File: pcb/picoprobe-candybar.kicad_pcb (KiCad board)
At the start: 2 copper layers, 27.9 x 95 mm, 50 parts, among them J0 SWD-UART_PicoprobeCandybar, J1 PinHeader_2x04, J2 PinSocket_1x03, J3 PinSocket_1x02, J4 PinSocket_1x03, J5 PinSocket_1x03, J6 PinSocket_1x03, J7 PinSocket_1x02, Q1 T2N7002AK, Q2 DMP31D1U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

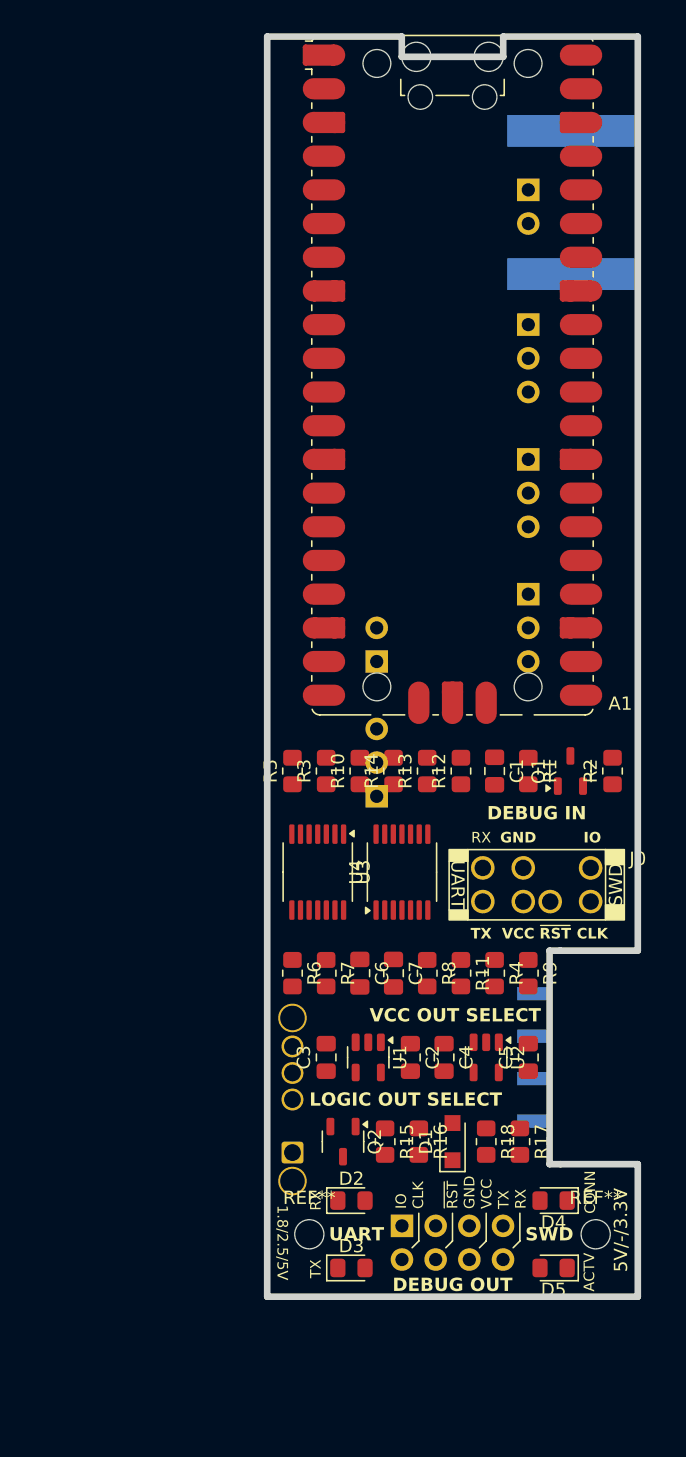
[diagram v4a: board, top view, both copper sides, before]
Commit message: Expand mounting hole copper clearance
Also adjusts some silkscreen text
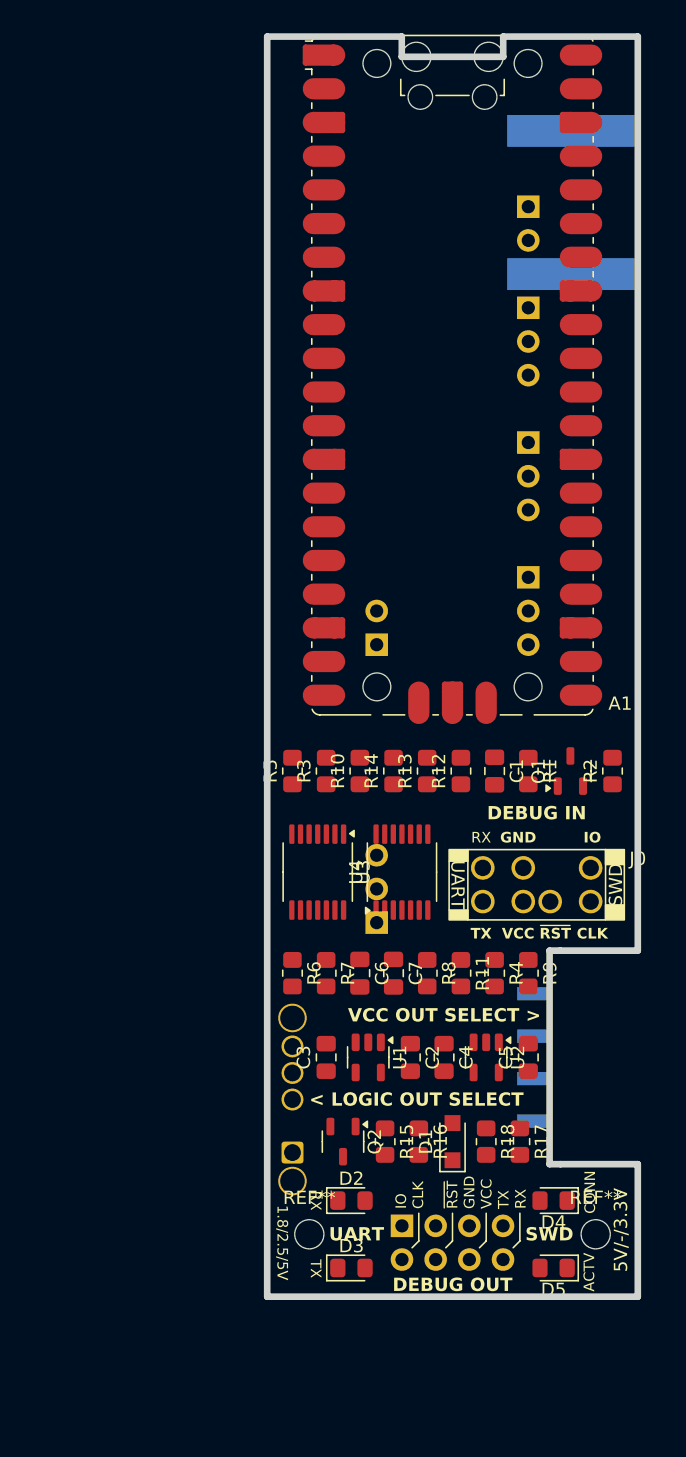
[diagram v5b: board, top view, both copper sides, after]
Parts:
- moved J2 9.53 mm to (95.9, 127.0)
- moved J6 1.27 mm to (107.3, 80.6)
- moved J7 1.27 mm to (107.3, 73.0)
- moved J3 1.27 mm to (95.9, 106.0)
- moved J4 1.27 mm to (107.3, 101.0)
- moved J5 1.27 mm to (107.3, 90.8)
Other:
- board text added: "< LOGIC OUT SELECT"
- board text added: "VCC OUT SELECT >"
- board text removed: "LOGIC OUT SELECT"
- board text removed: "VCC OUT SELECT"
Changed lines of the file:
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@@
 	)
 	(setup
+		(stackup
+			(layer "F.SilkS"
+				(type "Top Silk Screen")
+			)
+			(layer "F.Paste"
+				(type "Top Solder Paste")
+			)
+			(layer "F.Mask"
+				(type "Top Solder Mask")
+				(thickness 0.01)
+			)
+			(layer "F.Cu"
+				(type "copper")
+				(thickness 0.035)
+			)
+			(layer "dielectric 1"
+				(type "core")
+				(thickness 1.51)
+				(material "FR4")
+				(epsilon_r 4.5)
+				(loss_tangent 0.02)
+			)
+			(layer "B.Cu"
+				(type "copper")
+				(thickness 0.035)
+			)
+			(layer "B.Mask"
+				(type "Bottom Solder Mask")
+				(thickness 0.01)
+			)
+			(layer "B.Paste"
+				(type "Bottom Solder Paste")
+			)
+			(layer "B.SilkS"
+				(type "Bottom Silk Screen")
+			)
+			(copper_finish "None")
+			(dielectric_constraints no)
+		)
 		(pad_to_mask_clearance 0)
 		(allow_soldermask_bridges_in_footprints no)
@@
 		(fp_arc
 			(start 10.579676 25.189937)
-			(mid 10.357949 25.493953)
+			(mid 10.357946 25.493957)
 			(end 10 25.61)
 			(stroke
@@
 			(size 2.2 2.2)
 			(drill 2.2)
-			(layers "*.Cu" "*.Mask")
+			(layers "F&B.Cu" "*.Mask")
+			(clearance 0.9)
 		)
 	)
@@
 			(size 2.2 2.2)
 			(drill 2.2)
-			(layers "*.Cu" "*.Mask")
+			(layers "F&B.Cu" "*.Mask")
+			(clearance 0.9)
 		)
 	)
 	(footprint "Connector_PinSocket_2.54mm:PinSocket_1x03_P2.54mm_Horizontal"
 		(layer "B.Cu")
-		(at 107.315 81.915 180)
+		(at 107.315 80.645 180)
 		(descr "Through hole angled socket strip, 1x03, 2.54mm pitch, 8.51mm socket length, single row (from Kicad 4.0.7), script generated")
 		(tags "Through hole angled socket strip THT 1x03 2.54mm single row")
@@
 	(footprint "Connector_PinSocket_2.54mm:PinSocket_1x03_P2.54mm_Horizontal"
 		(layer "B.Cu")
-		(at 95.885 117.475)
+		(at 95.885 127)
 		(descr "Through hole angled socket strip, 1x03, 2.54mm pitch, 8.51mm socket length, single row (from Kicad 4.0.7), script generated")
 		(tags "Through hole angled socket strip THT 1x03 2.54mm single row")
@@
 	(footprint "Connector_PinSocket_2.54mm:PinSocket_1x03_P2.54mm_Horizontal"
 		(layer "B.Cu")
-		(at 107.315 92.075 180)
+		(at 107.315 90.805 180)
 		(descr "Through hole angled socket strip, 1x03, 2.54mm pitch, 8.51mm socket length, single row (from Kicad 4.0.7), script generated")
 		(tags "Through hole angled socket strip THT 1x03 2.54mm single row")
@@
 	(footprint "Connector_PinSocket_2.54mm:PinSocket_1x03_P2.54mm_Horizontal"
 		(layer "B.Cu")
-		(at 107.315 102.235 180)
+		(at 107.315 100.965 180)
 		(descr "Through hole angled socket strip, 1x03, 2.54mm pitch, 8.51mm socket length, single row (from Kicad 4.0.7), script generated")
 		(tags "Through hole angled socket strip THT 1x03 2.54mm single row")
@@
 	(footprint "Connector_PinSocket_2.54mm:PinSocket_1x02_P2.54mm_Horizontal"
 		(layer "B.Cu")
-		(at 107.315 71.755 180)
+		(at 107.315 73.025 180)
 		(descr "Through hole angled socket strip, 1x02, 2.54mm pitch, 8.51mm socket length, single row (from Kicad 4.0.7), script generated")
 		(tags "Through hole angled socket strip THT 1x02 2.54mm single row")
@@
 	(footprint "Connector_PinSocket_2.54mm:PinSocket_1x02_P2.54mm_Horizontal"
 		(layer "B.Cu")
-		(at 95.885 107.315)
+		(at 95.885 106.045)
 		(descr "Through hole angled socket strip, 1x02, 2.54mm pitch, 8.51mm socket length, single row (from Kicad 4.0.7), script generated")
 		(tags "Through hole angled socket strip THT 1x02 2.54mm single row")
@@
 	)
 	(gr_line
-		(start 115.57 145.21)
-		(end 115.57 155.198)
+		(start 109.73 145.21)
+		(end 115.57 145.21)
 		(stroke
 			(width 0.5)
@@
 	)
 	(gr_line
-		(start 109.73 145.21)
-		(end 115.57 145.21)
+		(start 97.775 60.198)
+		(end 97.775 61.725)
 		(stroke
 			(width 0.5)
@@
 	)
 	(gr_line
-		(start 97.775 60.198)
-		(end 97.775 61.725)
+		(start 105.425 60.198)
+		(end 105.425 61.725)
 		(stroke
 			(width 0.5)
@@
 	)
 	(gr_line
-		(start 97.775 61.725)
-		(end 105.425 61.725)
+		(start 115.57 145.21)
+		(end 115.57 155.198)
 		(stroke
 			(width 0.5)
@@
 	)
 	(gr_line
-		(start 105.425 60.198)
-		(end 115.57 60.198)
+		(start 97.775 61.725)
+		(end 105.425 61.725)
 		(stroke
 			(width 0.5)
@@
 	)
 	(gr_line
-		(start 105.425 60.198)
-		(end 105.425 61.725)
+		(start 109.73 129.11)
+		(end 115.57 129.11)
 		(stroke
 			(width 0.5)
@@
 	)
 	(gr_line
-		(start 109.73 129.11)
-		(end 115.57 129.11)
+		(start 105.425 60.198)
+		(end 115.57 60.198)
 		(stroke
 			(width 0.5)
@@
 		)
 	)
-	(gr_text "LOGIC OUT SELECT"
+	(gr_text "< LOGIC OUT SELECT"
 		(at 90.805 140.335 0)
 		(layer "F.SilkS")
@@
 	)
 	(gr_text "TX"
-		(at 91.7575 153.0985 90)
+		(at 91.7575 153.0985 270)
 		(layer "F.SilkS")
 		(effects
@@
 				(thickness 0.1)
 			)
-			(justify bottom)
+			(justify top)
 		)
 	)
 	(gr_text "RX"
-		(at 91.7575 147.955 90)
+		(at 91.7575 147.955 270)
 		(layer "F.SilkS")
 		(effects
@@
 				(thickness 0.1)
 			)
-			(justify bottom)
+			(justify top)
 		)
 	)
@@
 		)
 	)
-	(gr_text "VCC OUT SELECT"
+	(gr_text "VCC OUT SELECT >"
 		(at 108.2675 133.985 0)
 		(layer "F.SilkS")

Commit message: First pass trace layout (power & proximity)
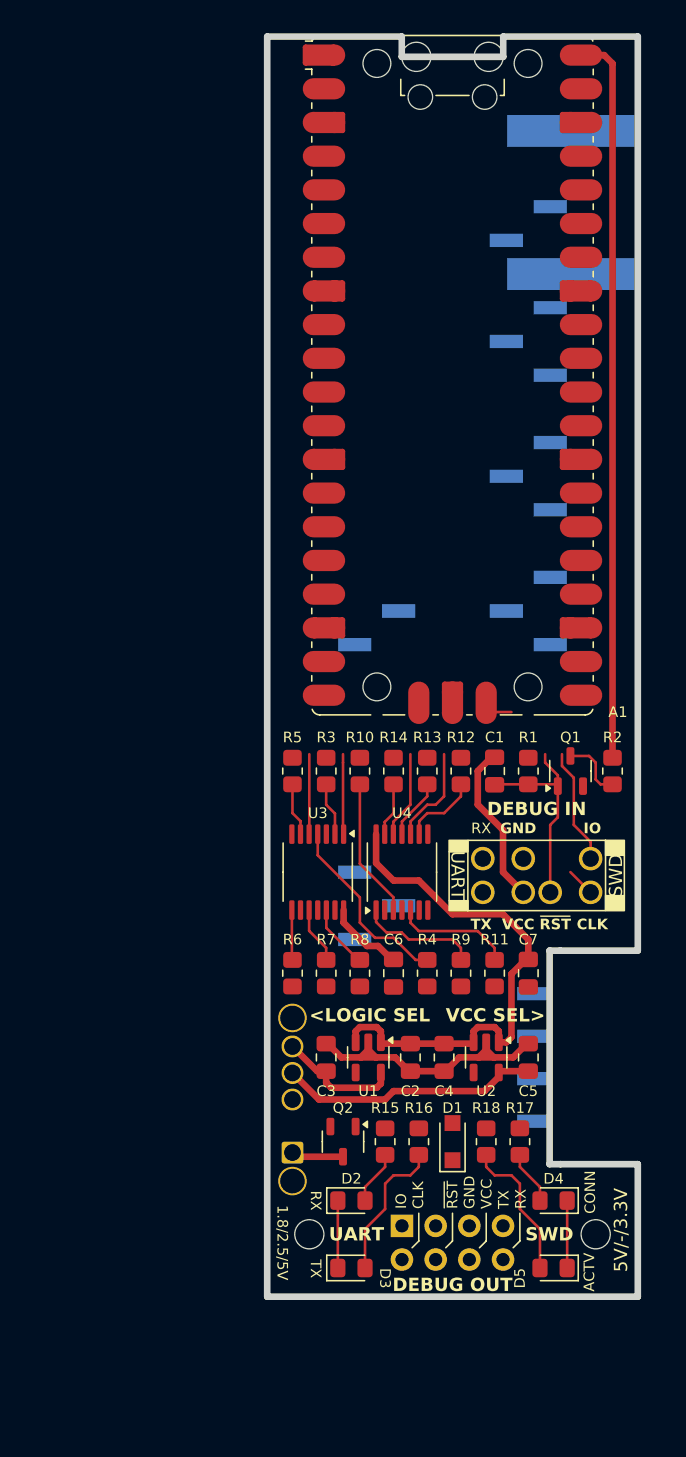
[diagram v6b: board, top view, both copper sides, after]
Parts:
- J2, J4, J5, J6: footprint Connector_PinSocket_2.54mm:PinSocket_1x03_P2.54mm_Horizontal -> Connector_PinHeader_2.54mm:PinHeader_1x03_P2.54mm_Vertical_SMD_Pin1Left
- J3, J7: footprint Connector_PinSocket_2.54mm:PinSocket_1x02_P2.54mm_Horizontal -> Connector_PinHeader_2.54mm:PinHeader_1x02_P2.54mm_Vertical_SMD_Pin1Left
- moved C7 10.2 mm to (107.3, 130.8)
- moved R4 5.08 mm to (99.7, 130.8)
- moved R8 5.08 mm to (94.6, 130.8)
- moved R9 5.08 mm to (102.2, 130.8)
- moved C6 2.54 mm to (97.2, 130.8)
- moved J6 2.54 mm to (107.3, 83.2)
- moved R11 2.54 mm to (104.8, 130.8)
- moved J4 2.54 mm to (107.3, 103.5)
- moved J5 2.54 mm to (107.3, 93.3)
- moved J2 1.27 mm to (95.9, 125.7)
- moved J3 1.27 mm to (95.9, 104.8)
- moved J7 1.27 mm to (107.3, 74.3)
- moved J0 0.70 mm to (111.8, 122.2)
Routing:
- net VBUS: track 0.00 -> 55.8 mm
- net 3V3: track 0.00 -> 39.9 mm
- net GND: track 0.00 -> 31.5 mm
- net 2V5: track 0.00 -> 19.7 mm
- net /3V3_EN: track 0.00 -> 15.9 mm
- net Net-(U3-2Y): track 0.00 -> 14.2 mm
- net VSYS: track 0.00 -> 12.3 mm
- net Net-(A1-SWDIO): track 0.00 -> 11.8 mm
- net Net-(D3-A): track 0.00 -> 10.9 mm
- net Net-(D5-A): track 0.00 -> 10.9 mm
- net Net-(U4-2A): track 0.00 -> 10.5 mm
- net 1V8: track 0.00 -> 9.43 mm
- net Net-(U4-1A): track 0.00 -> 9.01 mm
- net Net-(U4-3A): track 0.00 -> 8.99 mm
- net /GPIO18: track 0.00 -> 7.45 mm
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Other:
- board text added: "<LOGIC SEL"
- board text added: "VCC SEL>"
- board text removed: "< LOGIC OUT SELECT"
- board text removed: "VCC OUT SELECT >"

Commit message: Major rework (prioritize debug signal integrity)
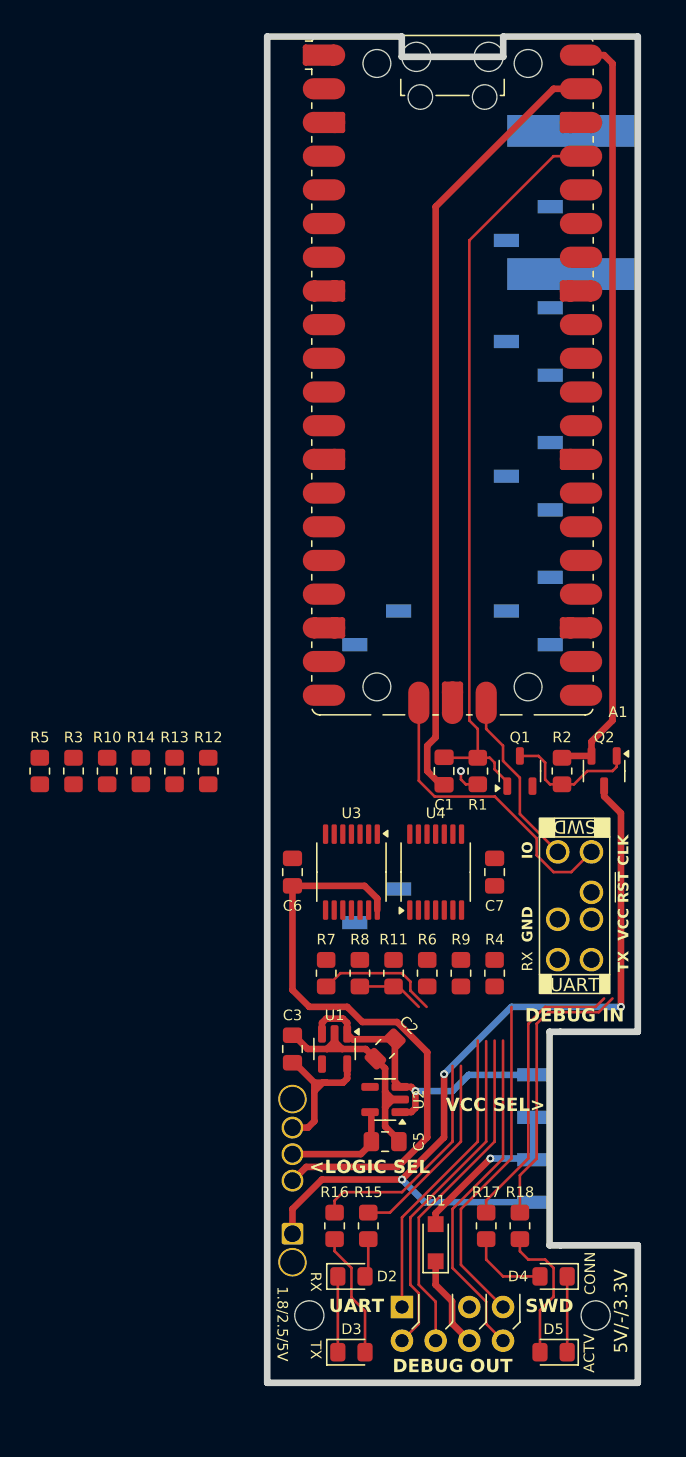
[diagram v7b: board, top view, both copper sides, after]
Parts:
- removed C4: 1u, Capacitor_SMD:C_0805_2012Metric_Pad1.18x1.45mm_HandSolder
- removed the REF** at (90.8, 150.5)
- removed the REF** at (112.4, 150.5)
- added REF**: MountingHole_2.2mm_M2_ISO7380, MountingHole:MountingHole_2.2mm_M2_ISO7380, F.Cu at (112.4, 156.6)
- added REF**: MountingHole_2.2mm_M2_ISO7380, MountingHole:MountingHole_2.2mm_M2_ISO7380, F.Cu at (90.8, 156.6)
- D5: value Orange -> Red
- J2: footprint Connector_PinHeader_2.54mm:PinHeader_1x03_P2.54mm_Vertical_SMD_Pin1Left -> Connector_PinSocket_2.54mm:PinSocket_1x02_P2.54mm_Vertical_SMD_Pin1Left
- J3, J7: footprint Connector_PinHeader_2.54mm:PinHeader_1x02_P2.54mm_Vertical_SMD_Pin1Left -> Connector_PinSocket_2.54mm:PinSocket_1x02_P2.54mm_Vertical_SMD_Pin1Left
- J4, J5, J6: footprint Connector_PinHeader_2.54mm:PinHeader_1x03_P2.54mm_Vertical_SMD_Pin1Left -> Connector_PinSocket_2.54mm:PinSocket_1x03_P2.54mm_Vertical_SMD_Pin1Left
- moved Q2 34.2 mm to (113.0, 115.6)
- moved R10 19.0 mm to (75.6, 115.6)
- moved R12 19.0 mm to (83.2, 115.6)
- moved R13 19.0 mm to (80.6, 115.6)
- moved R14 19.0 mm to (78.1, 115.6)
- moved R3 19.0 mm to (73.0, 115.6)
- moved R5 19.0 mm to (70.5, 115.6)
- moved C5 12.5 mm to (96.5, 143.5), turned to 0 degrees
- moved C6 10.8 mm to (89.5, 123.2), turned to 90 degrees
- moved R6 10.2 mm to (99.7, 130.8)
- moved R16 8.98 mm to (92.7, 149.9)
- moved U2 8.26 mm to (96.5, 140.3), turned to 180 degrees
- moved C7 8.03 mm to (104.8, 123.2)
- moved D1 7.73 mm to (100.3, 151.1)
- moved R11 7.62 mm to (97.2, 130.8)
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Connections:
- A1 pad 14: /GPIO10 -> /INT_RISE
- A1 pad 15: /GPIO11 -> /INT_FALL
- J3 pad 1: /GPIO11 -> /INT_RISE
- J3 pad 2: /GPIO10 -> /INT_FALL
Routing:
- net 5V: track 3.94 -> 63.5 mm, vias 0 -> 3
- net VSYS: track 12.3 -> 58.4 mm
- net /3V3_EN: track 15.9 -> 55.9 mm
- net VLOGIC: track 5.86 -> 45.6 mm
- net /CB_CLK: track 0.00 -> 35.2 mm
- net /CB_IO: track 0.00 -> 27.5 mm
- net /CB_RX: track 0.00 -> 25.8 mm
- net /CB_~{RST}: track 0.00 -> 25.5 mm
- net /CB_TX: track 0.00 -> 25.5 mm
- net /GPIO15: track 0.00 -> 22.1 mm
- net Net-(A1-SWCLK): track 2.16 -> 23.9 mm
- net /GPIO16: track 0.00 -> 21.3 mm
- net /GPIO9: track 0.00 -> 17.4 mm
- net 3V3: track 39.9 -> 24.6 mm, vias 0 -> 1
- net /GPIO8: track 0.00 -> 14.9 mm
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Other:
- board size 27.9 x 95 mm -> 27.9 x 101.5 mm
- board text removed: "IO CLK ~{RST} GND VCC TX RX"

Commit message: Incremental changes (prioritizing debug signal)
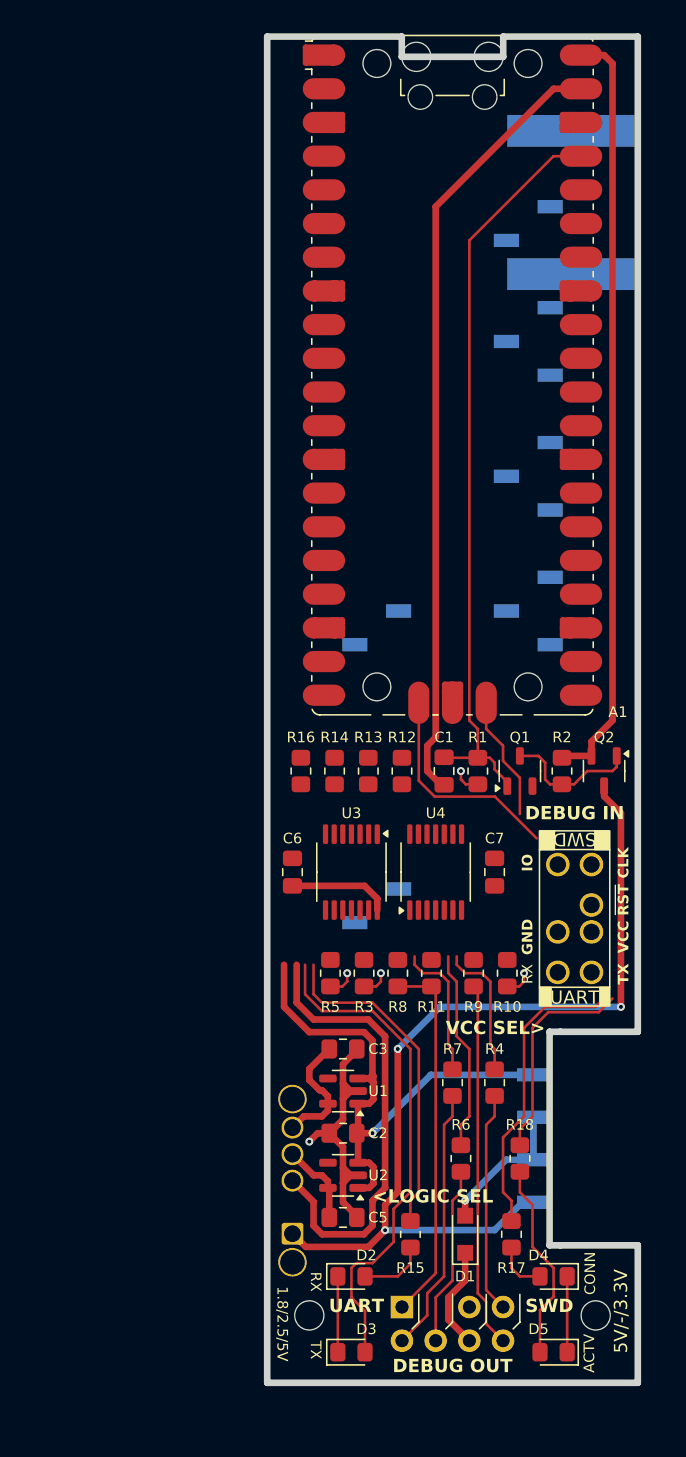
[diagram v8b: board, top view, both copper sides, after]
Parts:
- moved R16 34.4 mm to (90.2, 115.6)
- moved R10 33.8 mm to (105.7, 130.8), turned to -90 degrees
- moved R3 26.7 mm to (94.9, 130.8), turned to -90 degrees
- moved R5 26.7 mm to (92.4, 130.8), turned to -90 degrees
- moved R12 14.6 mm to (97.8, 115.6)
- moved R13 14.6 mm to (95.2, 115.6)
- moved R14 14.6 mm to (92.7, 115.6)
- moved R6 14.2 mm to (102.2, 144.8)
- moved R7 12.6 mm to (101.6, 139.1)
- moved R4 8.25 mm to (104.8, 139.1)
- moved C2 7.10 mm to (93.3, 142.9), turned to 180 degrees
- moved C5 6.54 mm to (93.3, 149.2)
- moved U2 6.54 mm to (93.3, 146.1)
- moved R18 5.08 mm to (106.7, 144.8)
- moved C3 3.81 mm to (93.3, 136.5), turned to 0 degrees
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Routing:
- net Net-(D3-A): track 9.48 -> 37.7 mm
- net /GPIO9: track 17.4 -> 0.00 mm
- net 3V3: track 24.6 -> 41.8 mm
- net Net-(U3-4Y): track 0.00 -> 15.2 mm
- net /CB_CLK: track 35.2 -> 20.0 mm
- net /CB_~{RST}: track 25.5 -> 13.5 mm
- net Net-(U3-2Y): track 0.00 -> 10.5 mm
- net Net-(U3-5Y): track 0.00 -> 10.5 mm
- net /GPIO8: track 14.9 -> 25.1 mm
- net /CB_TX: track 25.5 -> 16.7 mm
- net Net-(A1-SWCLK): track 23.9 -> 17.4 mm
- net 5V: track 63.5 -> 69.3 mm
- net /GPIO16: track 21.3 -> 16.2 mm
- net Net-(D5-A): track 10.7 -> 15.1 mm
- net Net-(A1-SWDIO): track 15.1 -> 11.1 mm
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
